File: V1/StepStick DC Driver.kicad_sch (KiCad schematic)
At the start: 10 parts, among them IC1 TB67H453FNG, IC2 TB67H453FNG, J1 Conn_01x08_Pin, J2 Conn_01x08_Pin

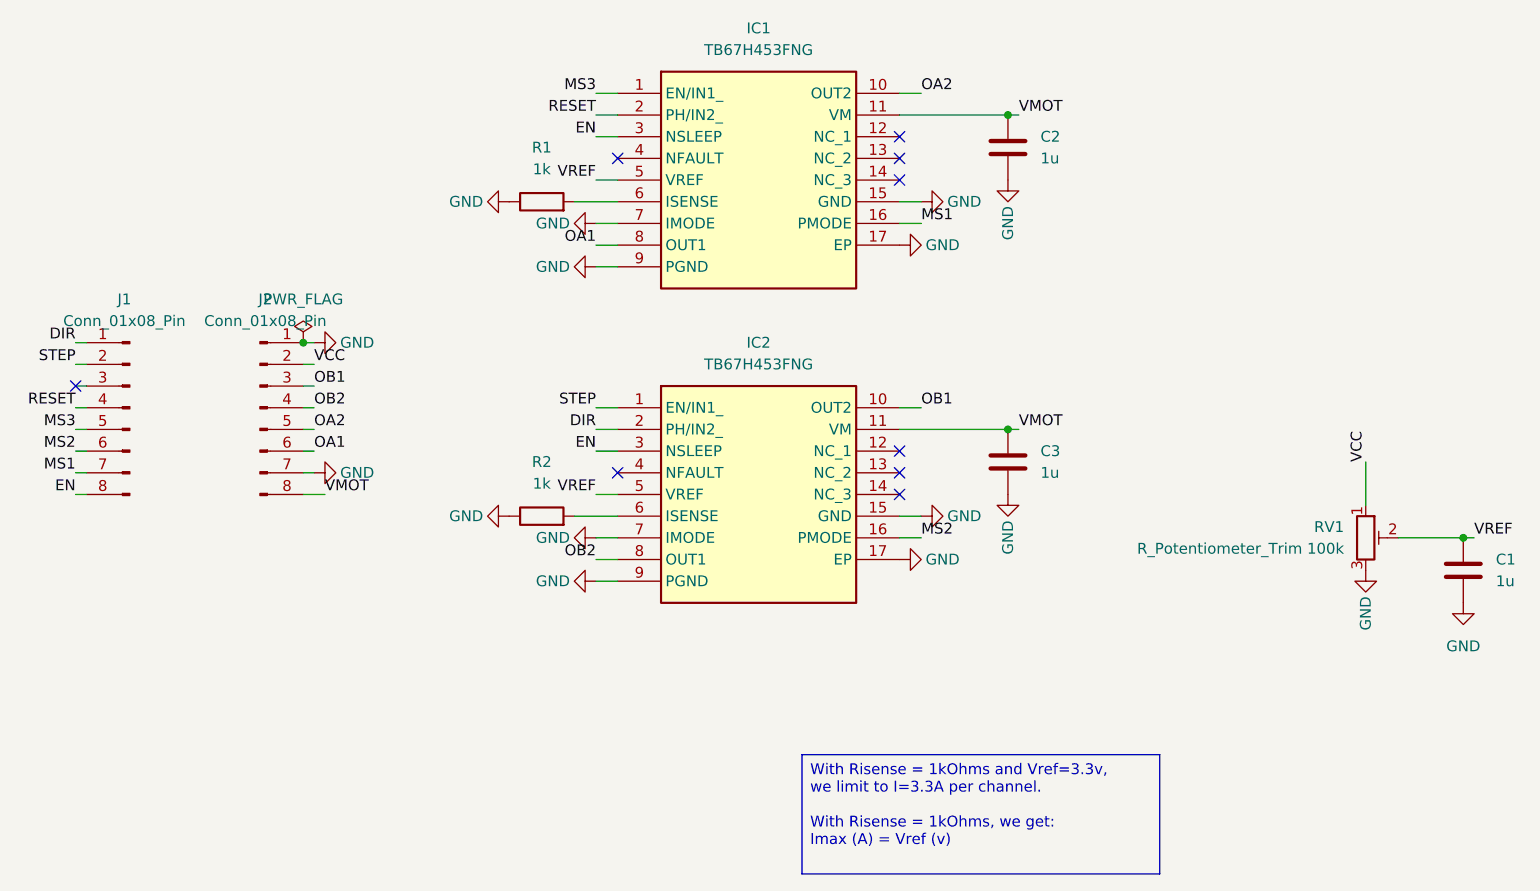
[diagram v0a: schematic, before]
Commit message: V2 Driver created, Moved V1 to subfolder
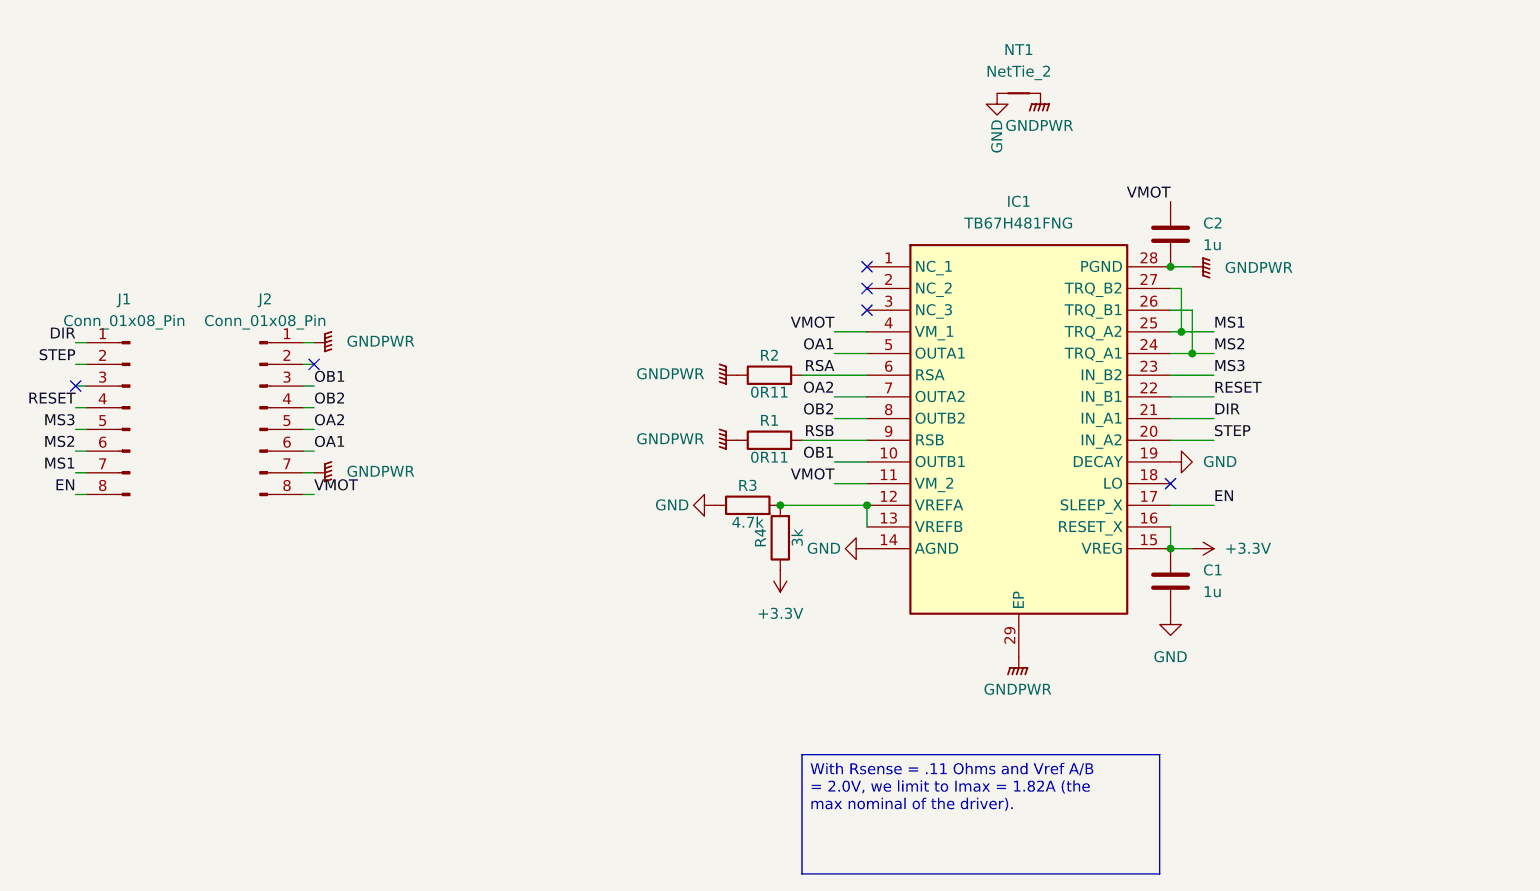
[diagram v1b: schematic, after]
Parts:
- removed C3: 1u, Capacitor_SMD:C_0805_2012Metric, symbol Device:C
- removed IC1, IC2: TB67H453FNG, TB67H453FNG:TB67H453FNG, symbol TB67H453FNG:TB67H453FNG
- removed RV1: R_Potentiometer_Trim 100k, POT_EVM3R:POT_EVM3R, symbol Device:R_Potentiometer_Trim
- added IC1: TB67H481FNG, TB67H481FNG:SOP65P640X120-29N, symbol TB67H481FNG:TB67H481FNG
- added NT1: NetTie_2, NetTie:NetTie-2_SMD_Pad0.5mm, symbol Device:NetTie_2
- added R3: 4.7k, Resistor_SMD:R_0805_2012Metric_Pad1.20x1.40mm_HandSolder, symbol Device:R
- added R4: 3k, Resistor_SMD:R_0805_2012Metric_Pad1.20x1.40mm_HandSolder, symbol Device:R
- C1, C2: footprint Capacitor_SMD:C_0805_2012Metric -> Capacitor_SMD:C_0805_2012Metric_Pad1.18x1.45mm_HandSolder
- R1, R2: value 1k -> 0R11
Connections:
- net DIR: now also IC1.21 (IN_A1)
- net EN: now also IC1.17 (SLEEP_X)
- net GND: now also IC1.14 (AGND), IC1.19 (DECAY), NT1.1, R3.1; no longer C2.1, J2.1 (Pin_1), J2.7 (Pin_7), R1.1, R2.1
- net MS1: now also IC1.25 (TRQ_A2), IC1.27 (TRQ_B2)
- net MS2: now also IC1.24 (TRQ_A1), IC1.26 (TRQ_B1)
- net MS3: now also IC1.23 (IN_B2)
- net OA1: now also IC1.5 (OUTA1)
- net OA2: now also IC1.7 (OUTA2)
- net OB1: now also IC1.10 (OUTB1)
- net OB2: now also IC1.8 (OUTB2)
- net RESET: now also IC1.22 (IN_B1)
- net STEP: now also IC1.20 (IN_A2)
- net VMOT: now also C2.1, IC1.11 (VM_2), IC1.4 (VM_1); no longer C2.2
- net RSA: now reaches R2.2
- net RSA: now also IC1.6 (RSA)
- net RSB: now reaches R1.2
- net RSB: now also IC1.9 (RSB)
- net VCC: no longer names the net of J2.2 (Pin_2)
- net VREF renamed +3.3V
- net +3.3V: now also IC1.15 (VREG), IC1.16 (RESET_X), R4.1
- new net: IC1.12 (VREFA), IC1.13 (VREFB), R3.2, R4.2
- new net GNDPWR: C2.2, IC1.28 (PGND), IC1.29 (EP), J2.1 (Pin_1), J2.7 (Pin_7), NT1.2, R1.1, R2.1
- no-connect marks 9 -> 6
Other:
- moved on the sheet: C1
